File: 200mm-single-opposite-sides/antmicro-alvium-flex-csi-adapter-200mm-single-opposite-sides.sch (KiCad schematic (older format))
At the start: 3 parts, among them J1 WE_687622100002_FLEX, J2 WE_687650100002_FLEX

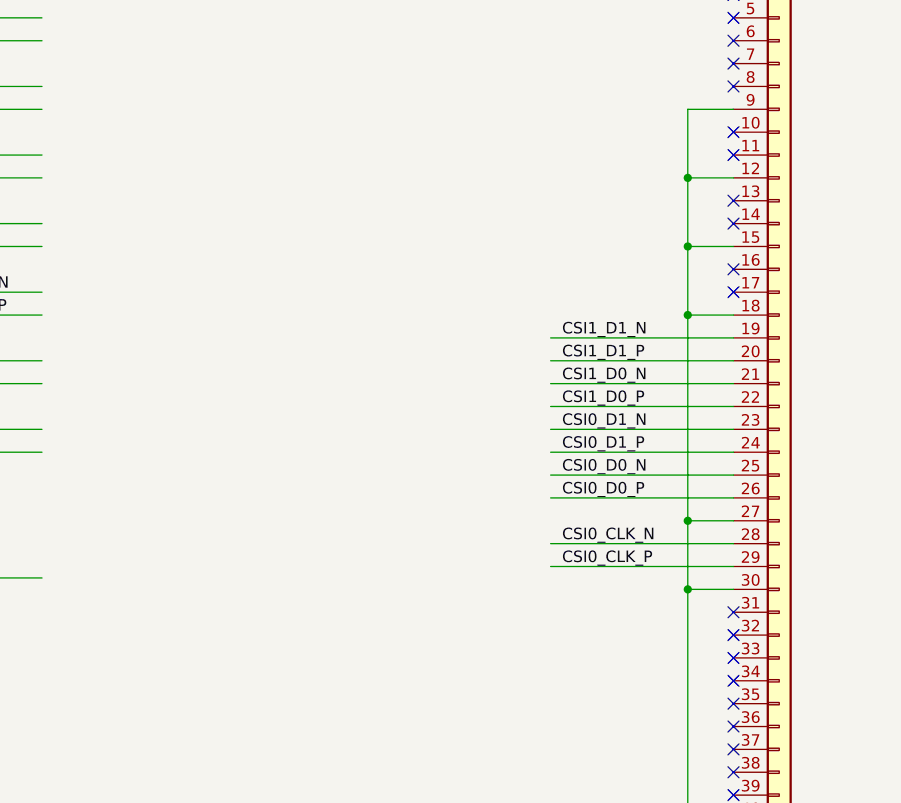
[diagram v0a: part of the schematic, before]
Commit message: 200mm-single-opposite: add NMOS transistor for camera triggering
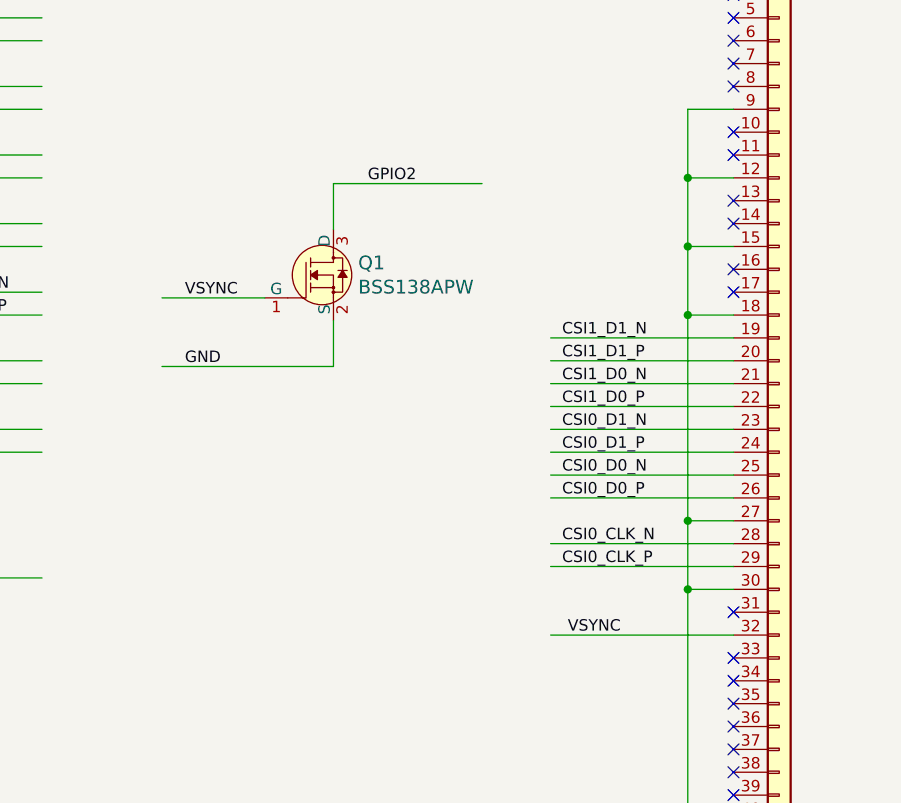
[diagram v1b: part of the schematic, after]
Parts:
- added Q1: BSS138APW, antmicro-alvium-flex-csi-adapter-footprints:SC70-3, symbol antmicro-alvium-flex-csi-adapter:BSS138APW
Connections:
- net labels added: VSYNC
- wire segments 61 -> 67
- no-connect marks 30 -> 29
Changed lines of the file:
@@
 EndData
 $EndBitmap
-NoConn ~ 9900 6575
 $Bitmap
 Pos 3150 10700
@@
 	1    0    0    -1
 $EndComp
+$Comp
+L antmicro-alvium-flex-csi-adapter:BSS138APW Q1
+U 1 1 5F887284
+P 8150 5000
+F 0 "Q1" H 8258 5053 60  0000 L CNN
+F 1 "BSS138APW" H 8258 4947 60  0000 L CNN
+F 2 "antmicro-alvium-flex-csi-adapter-footprints:SC70-3" H 8350 5200 60  0001 L CNN
+F 3 "" H 8350 5300 60  0001 L CNN
+F 4 "BSS138PW" H 8350 5500 60  0001 L CNN "MPN"
+F 5 "ON Semiconductor" H 8350 6100 60  0001 L CNN "Manufacturer"
+	1    8150 5000
+	1    0    0    -1
+$EndComp
+Wire Wire Line
+	8150 5200 8150 5400
+Wire Wire Line
+	8150 5400 7400 5400
+Wire Wire Line
+	7850 5100 7400 5100
+Wire Wire Line
+	8150 4800 8150 4600
+Wire Wire Line
+	8150 4600 8800 4600
+Text Label 7500 5400 0    50   ~ 0
+GND
+Text Label 8300 4600 0    50   ~ 0
+GPIO2
+Text Label 7500 5100 0    50   ~ 0
+VSYNC
+Wire Wire Line
+	9900 6575 9100 6575
+Text Label 9175 6575 0    50   ~ 0
+VSYNC
 $EndSCHEMATC
